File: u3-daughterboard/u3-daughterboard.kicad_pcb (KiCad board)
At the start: 2 copper layers, 40 x 9 mm, 9 parts, among them J1 USB_C_Receptacle_USB2.0, J2 Conn_01x06_MountingPin, U1 USBLC6-2P6

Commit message: Finish U3 daughterboard production files
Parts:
- added C1: 100nF, Capacitor_SMD:C_0402_1005Metric, F.Cu at (100.4, 90.5)
- added REF**: Tab, KiKit:Tab, F.Cu at (101.5, 93.0)
- moved R2 1.39 mm to (97.8, 88.8)
- moved R1 1.24 mm to (97.8, 87.7)
- moved D1 0.47 mm to (102.1, 90.5)
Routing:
- net Net-(J1-CC2): track 12.0 -> 11.5 mm
- net Net-(J1-CC1): track 15.5 -> 15.0 mm
- net GND: track 4.23 -> 4.49 mm, vias 5 -> 4

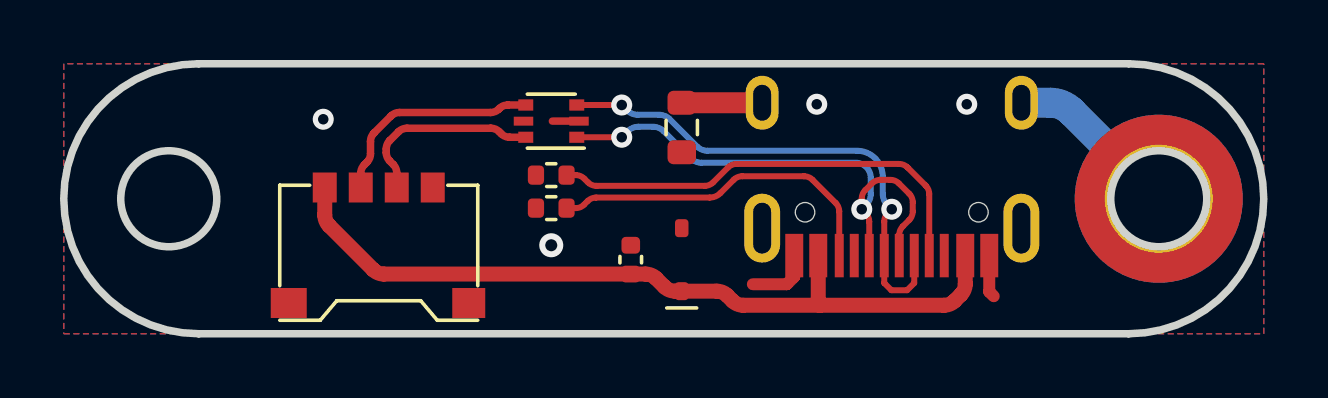
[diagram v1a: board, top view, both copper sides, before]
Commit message: Update U3 design files and add production files
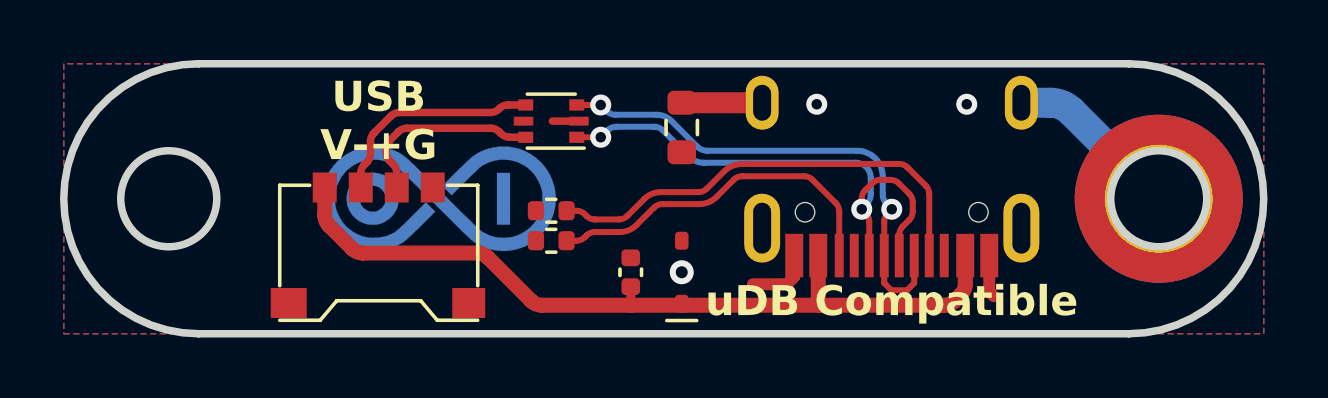
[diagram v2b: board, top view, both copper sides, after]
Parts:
- added G***: LOGO, BIOI:mini_logo, B.Cu at (94.0, 88.5)
- moved R1 1.19 mm to (97.8, 88.9)
- moved R2 1.09 mm to (97.8, 89.9)
- moved C1 0.42 mm to (100.4, 91.0)
- moved D1 0.42 mm to (102.1, 91.0)
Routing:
- net UVCC: track 26.5 -> 27.1 mm
- net GND: vias 4 -> 3
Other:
- board text added: "USB V-+G"
- board text added: "uDB Compatible"
